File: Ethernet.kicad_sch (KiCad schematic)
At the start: 7 parts, among them J2 RJ45_LINK-PP_LPJG0926HENL_Hor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, U14 TPD4EUSB30, U15 TPD4EUSB30

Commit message: Weeded out all ERC errors
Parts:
- C401: renamed from C31; value 100n -> 100nF; LCSC (none) -> C1525
- C402: renamed from C32; value 1n/1kV -> 1nF/1kV; LCSC (none) -> C1941
- J401: renamed from J2; value RJ45_LINK-PP_LPJG0926HENL_Horizontal -> HC915320A-909-A; footprint Yellow:RJ45_LINK-PP_LPJG0926HENL_Horizontal -> Hatlabs:RJ45_HC915320A-909-A_Vertical; LCSC (none) -> C5341220; Manufacturer LINK-PP -> (none); Notes (none) -> Alt. LPJG0926HENL; PartNumber LPJG0926HENL -> HC915320A-909-A
- R401: renamed from R22; LCSC (none) -> C25117
- R402: renamed from R23; LCSC (none) -> C25117
- U401: renamed from U14; LCSC (none) -> C558427
- U402: renamed from U15; LCSC (none) -> C558427; Manufacturer Texas Instruments -> (none)
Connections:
- net +3V3 renamed CMx_3V3
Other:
- company: Nabu Casa -> Hat Labs Oy
- title: Ethernet -> HALPI2
- moved on the sheet: C402

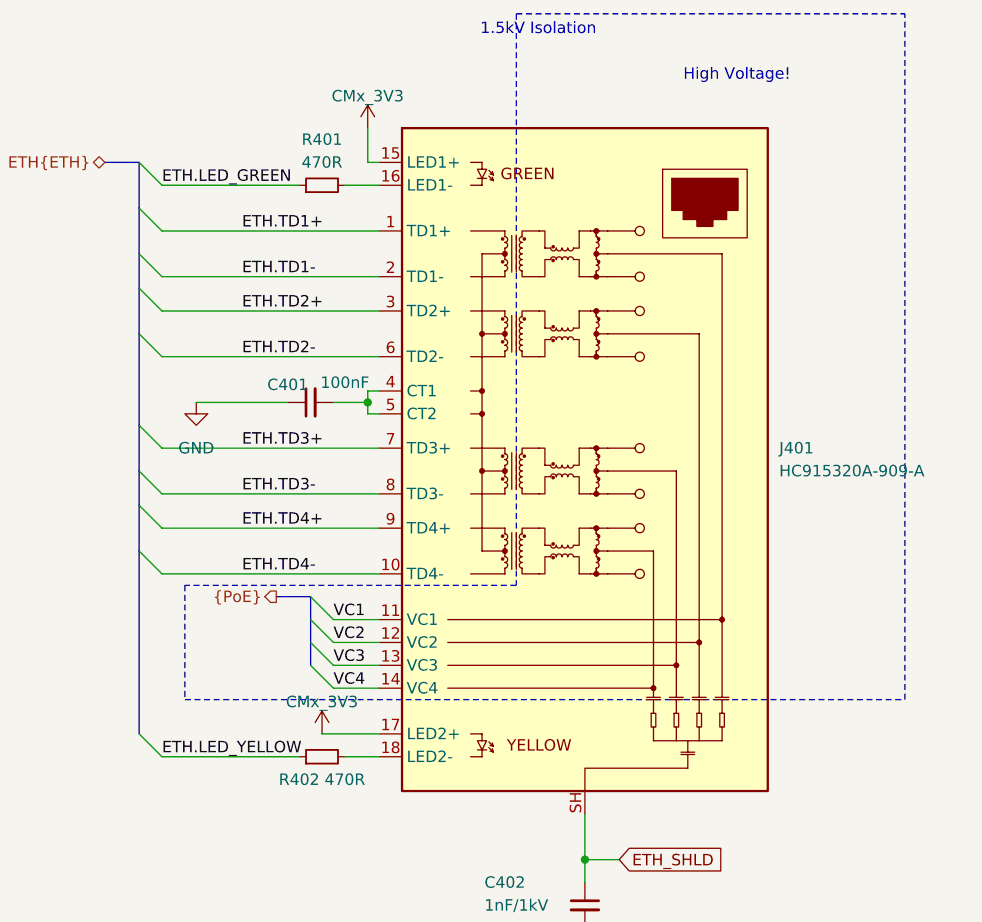
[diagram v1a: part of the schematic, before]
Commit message: Fix ethernet port & other changes
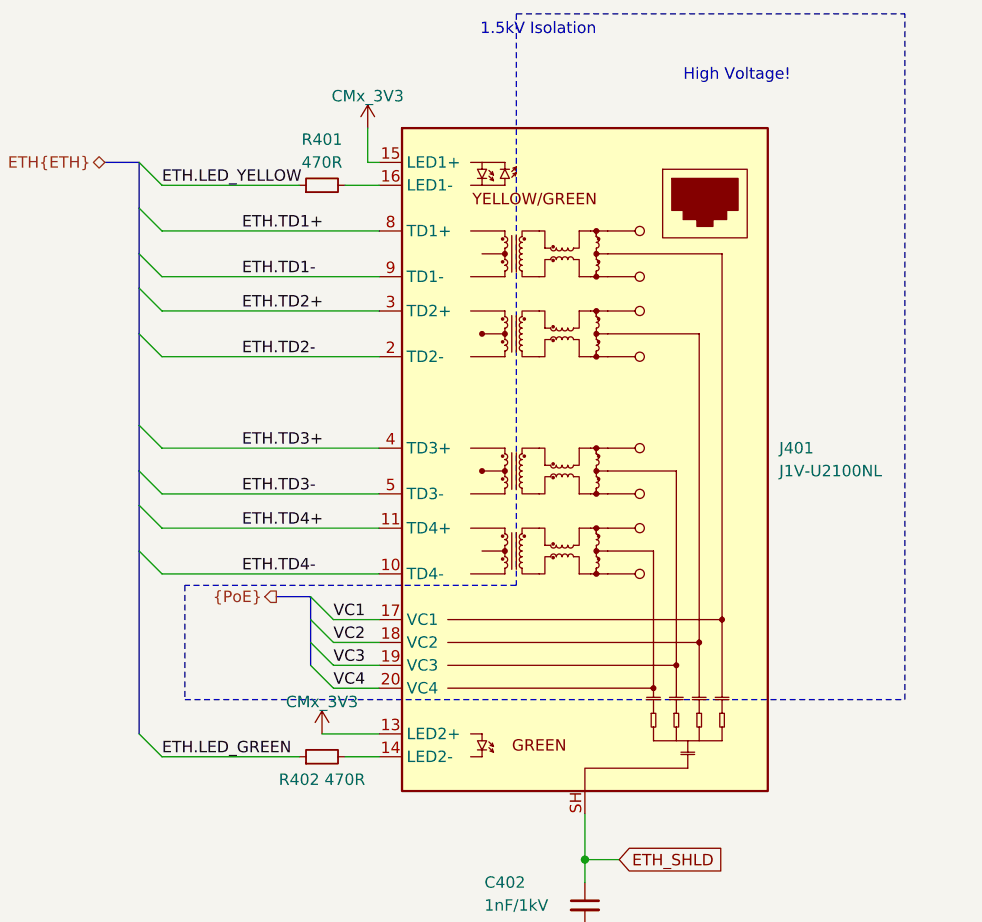
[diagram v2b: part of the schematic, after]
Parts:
- removed C401: 100nF, Capacitor_SMD:C_0402_1005Metric, symbol Device:C_Small
- J401: value HC915320A-909-A -> J1V-U2100NL; footprint Hatlabs:RJ45_HC915320A-909-A_Vertical -> Hatlabs:RJ45_Pulse_J1V_U2100NL_Vertical; symbol Yellow:RJ45_LINK-PP_LPJG0926HENL_Horizontal -> Hatlabs:RJ45_Pulse_J1V-U2100NL_Vertical; LCSC C5341220 -> C3179838; Notes Alt. LPJG0926HENL -> (none); PartNumber HC915320A-909-A -> (none)
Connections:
- net CMx_3V3: now also J401.13 (LED2+); no longer J401.17 (LED2+)
- net ETH.LED_GREEN: now also R402.1; no longer R401.1
- net ETH.LED_YELLOW: now also R401.1; no longer R402.1
- net ETH.TD1+: now also J401.8 (TD1+); no longer J401.1 (TD1+)
- net ETH.TD1-: now also J401.9 (TD1-); no longer J401.2 (TD1-)
- net ETH.TD2-: now also J401.2 (TD2-); no longer J401.6 (TD2-)
- net ETH.TD3+: now also J401.4 (TD3+); no longer J401.7 (TD3+)
- net ETH.TD3-: now also J401.5 (TD3-); no longer J401.8 (TD3-)
- net ETH.TD4+: now also J401.11 (TD4+); no longer J401.9 (TD4+)
- net VC1: now also J401.17 (VC1); no longer J401.11 (VC1)
- net VC2: now also J401.18 (VC2); no longer J401.12 (VC2)
- net VC3: now also J401.19 (VC3); no longer J401.13 (VC3)
- net VC4: now also J401.20 (VC4); no longer J401.14 (VC4)
- net at R402.2: now also J401.14 (LED2-); no longer J401.18 (LED2-)
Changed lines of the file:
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@@
-		(color 0 0 0 0)
-	)
-	(junction
-		(at 153.67 80.01)
-		(diameter 0.9144)
 		(color 0 0 0 0)
 	)
@@
 	(wire
 		(pts
-			(xy 134.62 80.01) (xy 144.78 80.01)
-		)
-		(stroke
-			(width 0)
-			(type solid)
-		)
-	)
-	(wire
-		(pts
 			(xy 130.81 55.88) (xy 146.05 55.88)
 		)
@@
 		)
 	)
-	(wire
-		(pts
-			(xy 153.67 81.28) (xy 154.94 81.28)
-		)
-		(stroke
-			(width 0)
-			(type solid)
-		)
-	)
 	(polyline
 		(pts
@@
 	(wire
 		(pts
-			(xy 153.67 78.74) (xy 153.67 80.01)
-		)
-		(stroke
-			(width 0)
-			(type solid)
-		)
-	)
-	(wire
-		(pts
 			(xy 130.81 66.04) (xy 154.94 66.04)
 		)
@@
 		)
 	)
-	(wire
-		(pts
-			(xy 149.86 80.01) (xy 153.67 80.01)
-		)
-		(stroke
-			(width 0)
-			(type solid)
-		)
-	)
 	(bus
 		(pts
@@
 			(width 0)
 			(type dash)
-		)
-	)
-	(wire
-		(pts
-			(xy 153.67 80.01) (xy 153.67 81.28)
-		)
-		(stroke
-			(width 0)
-			(type solid)
-		)
-	)
-	(wire
-		(pts
-			(xy 154.94 78.74) (xy 153.67 78.74)
-		)
-		(stroke
-			(width 0)
-			(type solid)
 		)
 	)
@@
 		)
 	)
-	(label "ETH.LED_YELLOW"
+	(label "ETH.LED_GREEN"
 		(at 130.81 119.38 0)
 		(fields_autoplaced yes)
@@
 		)
 	)
-	(label "ETH.LED_GREEN"
+	(label "ETH.LED_YELLOW"
 		(at 130.81 55.88 0)
 		(fields_autoplaced yes)
@@
 	)
 	(symbol
-		(lib_id "Yellow:RJ45_LINK-PP_LPJG0926HENL_Horizontal")
+		(lib_id "Hatlabs:RJ45_Pulse_J1V-U2100NL_Vertical")
 		(at 177.8 86.36 0)
 		(unit 1)
@@
 			)
 		)
-		(property "Value" "HC915320A-909-A"
+		(property "Value" "J1V-U2100NL"
 			(at 199.39 87.6299 0)
 			(effects
@@
 			)
 		)
-		(property "Footprint" "Hatlabs:RJ45_HC915320A-909-A_Vertical"
-			(at 177.8 132.08 0)
-			(effects
-				(font
-					(size 1.27 1.27)
-				)
-				(hide yes)
-			)
-		)
-		(property "Datasheet" "https://www.lcsc.com/datasheet/lcsc_datasheet_2306200940_HCTL-HC915320A-909-A_C5341220.pdf"
-			(at 177.8 132.08 0)
-			(effects
-				(font
-					(size 1.27 1.27)
-				)
-				(hide yes)
-			)
-		)
-		(property "Description" ""
-			(at 177.8 86.36 0)
+		(property "Footprint" "Hatlabs:RJ45_Pulse_J1V_U2100NL_Vertical"
+			(at 177.8 133.35 0)
+			(effects
+				(font
+					(size 1.27 1.27)
+				)
+				(hide yes)
+			)
+		)
+		(property "Datasheet" ""
+			(at 177.8 133.35 0)
+			(effects
+				(font
+					(size 1.27 1.27)
+				)
+				(hide yes)
+			)
+		)
+		(property "Description" "1 Port RJ45 Magjack Connector Through Hole 10/100/1000 Base-T, AutoMDIX"
+			(at 178.054 42.418 0)
 			(effects
 				(font
@@
 			)
 		)
-		(property "PartNumber" "HC915320A-909-A"
+		(property "PartNumber" ""
 			(at 177.8 86.36 0)
 			(effects
@@
 			)
 		)
-		(property "Notes" "Alt. LPJG0926HENL"
+		(property "Notes" ""
 			(at 177.8 86.36 0)
 			(effects
@@
 			)
 		)
-		(property "LCSC" "C5341220"
+		(property "LCSC" "C3179838"
 			(at 177.8 86.36 0)
 			(effects
@@
 		)
 		(pin "SH"
+		)
+		(pin "19"
+		)
+		(pin "20"
 		)
 		(instances
@@
 				(path "/abc482bd-3f17-4d35-80db-1da3dcdb5c27/18c18357-12fa-4472-a108-e954e5bd7840"
 					(reference "#PWR0406")
-					(unit 1)
-				)
-			)
-		)
-	)
-	(symbol
-		(lib_id "Device:C_Small")
-		(at 147.32 80.01 90)
-		(unit 1)
-		(exclude_from_sim no)
-		(in_bom yes)
-		(on_board yes)
-		(dnp no)
-		(property "Reference" "C401"
-			(at 144.78 78.0477 90)
-			(effects
-				(font
-					(size 1.27 1.27)
-				)
-			)
-		)
-		(property "Value" "100nF"
-			(at 151.13 77.806 90)
-			(effects
-				(font
-					(size 1.27 1.27)
-				)
-			)
-		)
-		(property "Footprint" "Capacitor_SMD:C_0402_1005Metric"
-			(at 147.32 80.01 0)
-			(effects
-				(font
-					(size 1.27 1.27)
-				)
-				(hide yes)
-			)
-		)
-		(property "Datasheet" "~"
-			(at 147.32 80.01 0)
-			(effects
-				(font
-					(size 1.27 1.27)
-				)
-				(hide yes)
-			)
-		)
-		(property "Description" ""
-			(at 147.32 80.01 0)
-			(effects
-				(font
-					(size 1.27 1.27)
-				)
-				(hide yes)
-			)
-		)
-		(property "LCSC" "C1525"
-			(at 147.32 80.01 0)
-			(effects
-				(font
-					(size 1.27 1.27)
-				)
-				(hide yes)
-			)
-		)
-		(property "Sim.Enable" ""
-			(at 147.32 80.01 0)
-			(effects
-				(font
-					(size 1.27 1.27)
-				)
-				(hide yes)
-			)
-		)
-		(pin "1"
-		)
-		(pin "2"
-		)
-		(instances
-			(project "Yellow"
-				(path "/abc482bd-3f17-4d35-80db-1da3dcdb5c27/18c18357-12fa-4472-a108-e954e5bd7840"
-					(reference "C401")
 					(unit 1)
 				)
@@
 					(unit 1)
 				)
-			)
-		)
-	)
-	(symbol
-		(lib_id "power:GND")
-		(at 134.62 80.01 0)
-		(unit 1)
-		(exclude_from_sim no)
-		(in_bom yes)
-		(on_board yes)
-		(dnp no)
-		(fields_autoplaced yes)
-		(property "Reference" "#PWR0403"
-			(at 134.62 86.36 0)
-			(effects
-				(font
-					(size 1.27 1.27)
-				)
-				(hide yes)
-			)
-		)
-		(property "Value" "GND"
-			(at 134.62 85.09 0)
-			(effects
-				(font
-					(size 1.27 1.27)
-				)
-			)
-		)
-		(property "Footprint" ""
-			(at 134.62 80.01 0)
-			(effects
-				(font
-					(size 1.27 1.27)
-				)
-				(hide yes)
-			)
-		)
-		(property "Datasheet" ""
-			(at 134.62 80.01 0)
-			(effects
-				(font
-					(size 1.27 1.27)
-				)
-				(hide yes)
-			)
-		)
-		(property "Description" "Power symbol creates a global label with name \"GND\" , ground"
-			(at 134.62 80.01 0)
-			(effects
-				(font
-					(size 1.27 1.27)
-				)
-				(hide yes)
-			)
-		)
-		(pin "1"
-		)
-		(instances
-			(project "Yellow"
-				(path "/abc482bd-3f17-4d35-80db-1da3dcdb5c27/18c18357-12fa-4472-a108-e954e5bd7840"
-					(reference "#PWR0403")
-					(unit 1)
-				)

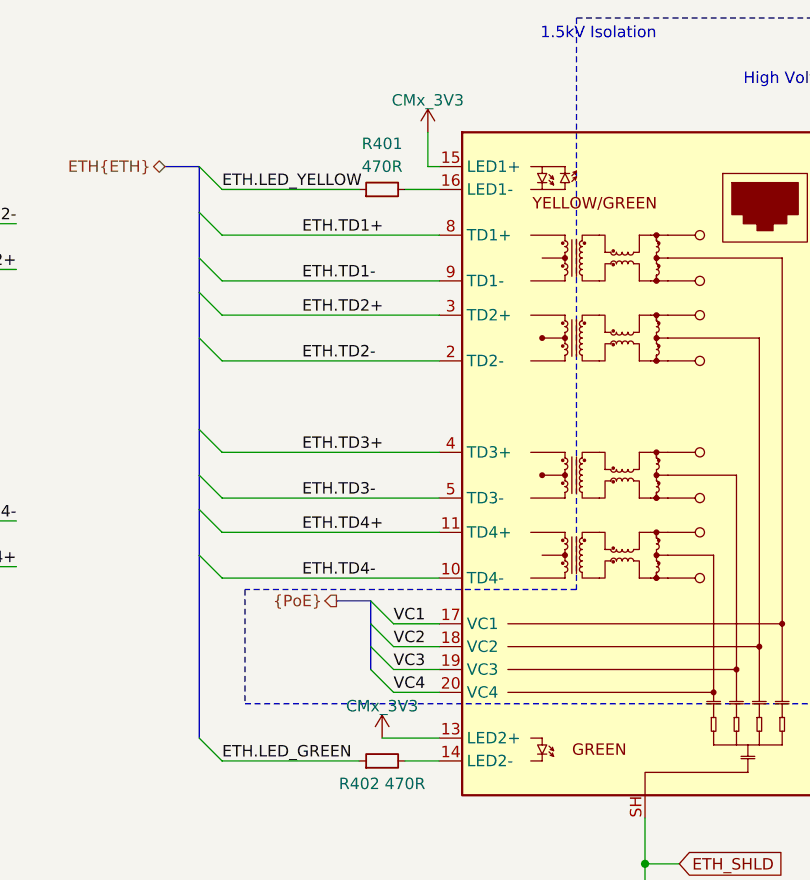
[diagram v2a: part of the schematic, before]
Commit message: Implement a USB3 hub
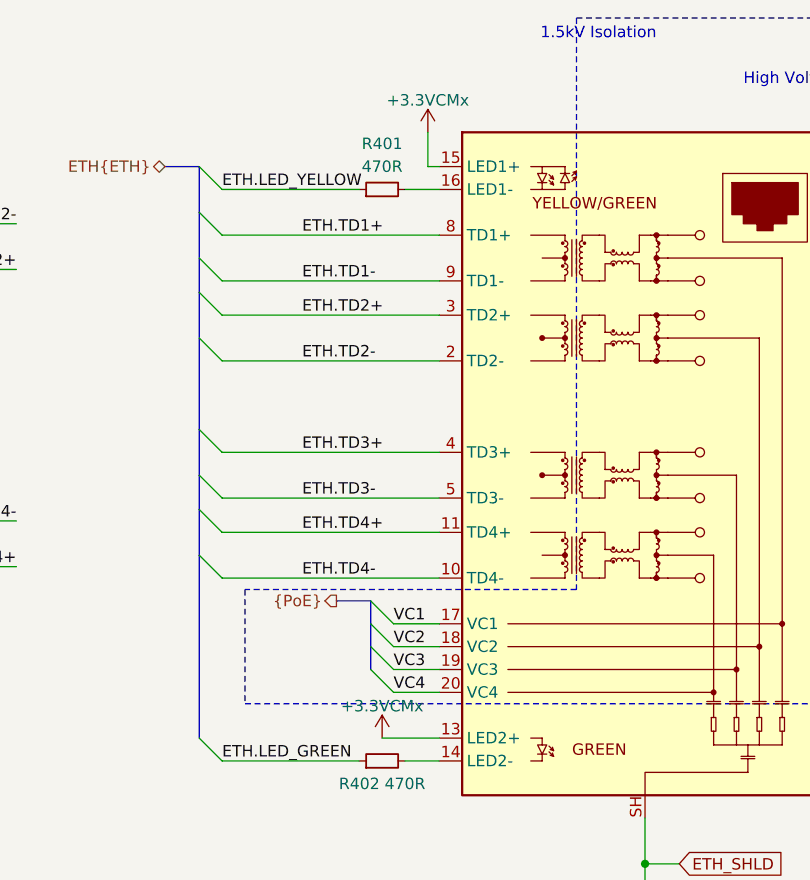
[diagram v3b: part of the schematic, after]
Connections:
- net CMx_3V3 renamed +3.3VCMx
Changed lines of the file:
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@@
 	)
 	(symbol
-		(lib_id "power:+3V3")
+		(lib_id "Hatlabs:+3.3VCMx")
 		(at 148.59 116.84 0)
 		(unit 1)
@@
 			)
 		)
-		(property "Value" "CMx_3V3"
+		(property "Value" "+3.3VCMx"
 			(at 148.59 113.284 0)
 			(effects
@@
 			)
 		)
-		(property "Description" "Power symbol creates a global label with name \"CMx_3V3\""
+		(property "Description" "Power symbol driven by the CMx module +3.3V output"
 			(at 148.59 116.84 0)
 			(effects
@@
 	)
 	(symbol
-		(lib_id "power:+3V3")
+		(lib_id "Hatlabs:+3.3VCMx")
 		(at 153.67 49.53 0)
 		(unit 1)
@@
 			)
 		)
-		(property "Value" "CMx_3V3"
+		(property "Value" "+3.3VCMx"
 			(at 153.67 45.974 0)
 			(effects
@@
 			)
 		)
-		(property "Description" "Power symbol creates a global label with name \"CMx_3V3\""
+		(property "Description" "Power symbol driven by the CMx module +3.3V output"
 			(at 153.67 49.53 0)
 			(effects
